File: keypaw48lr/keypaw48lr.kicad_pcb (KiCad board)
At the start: 2 copper layers, 139 x 102 mm, 108 parts, among them J1 Conn_01x02, J2 Conn_01x02, J3 Conn_01x02, J4 Conn_01x02, J5 Conn_01x02, J6 JD9613_OLED_FPC_Conn_01x10, J7 JD9613_OLED_FPC_Conn_01x10, J8 DXCL_S2002A_C, SW1 SW_SPDT, U1 nice_nano, U2 PAW3395, U3 TLV70019_SOT23-5, U4 TPS22917DBV

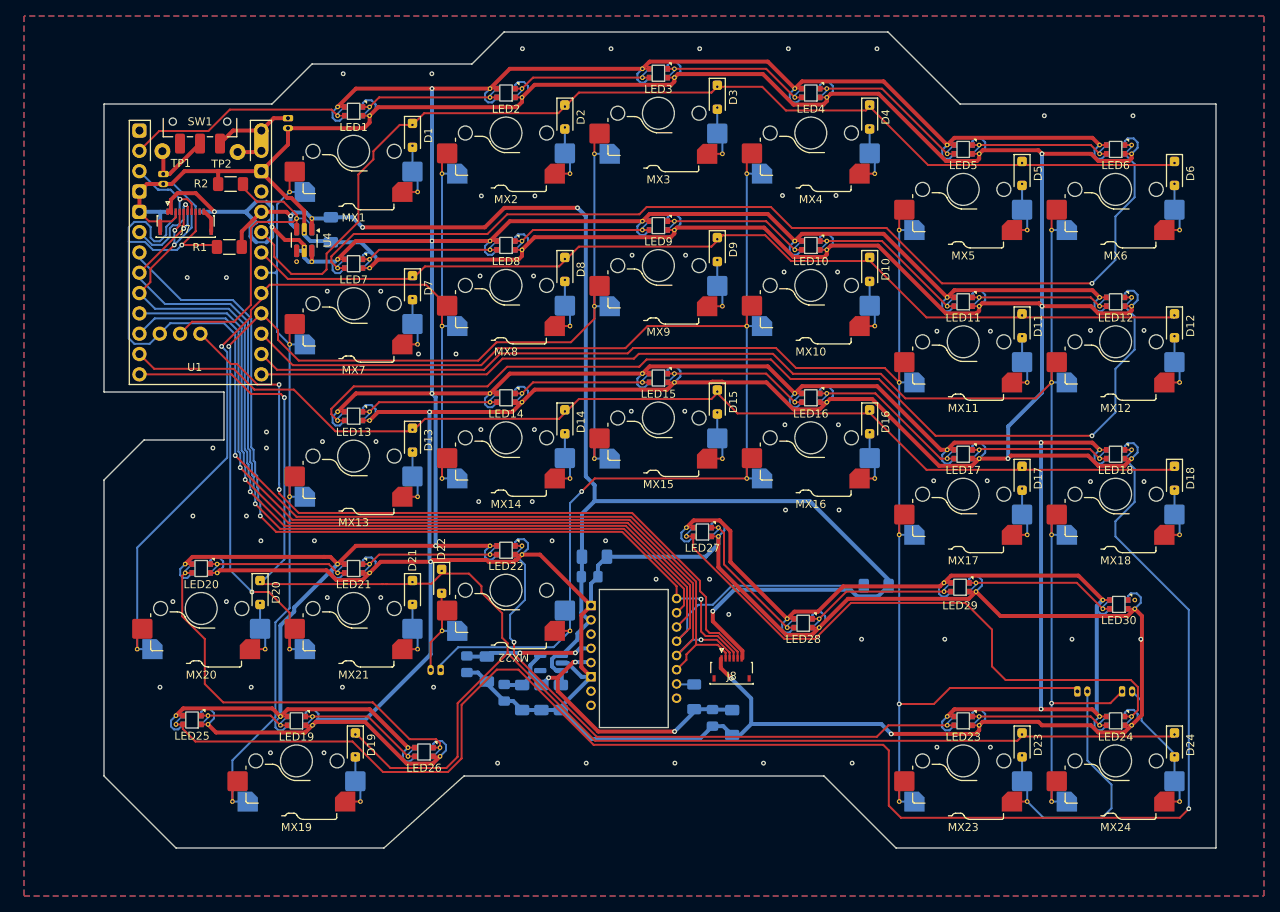
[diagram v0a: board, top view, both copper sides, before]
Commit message: feat: modify pcb for a simple box casing
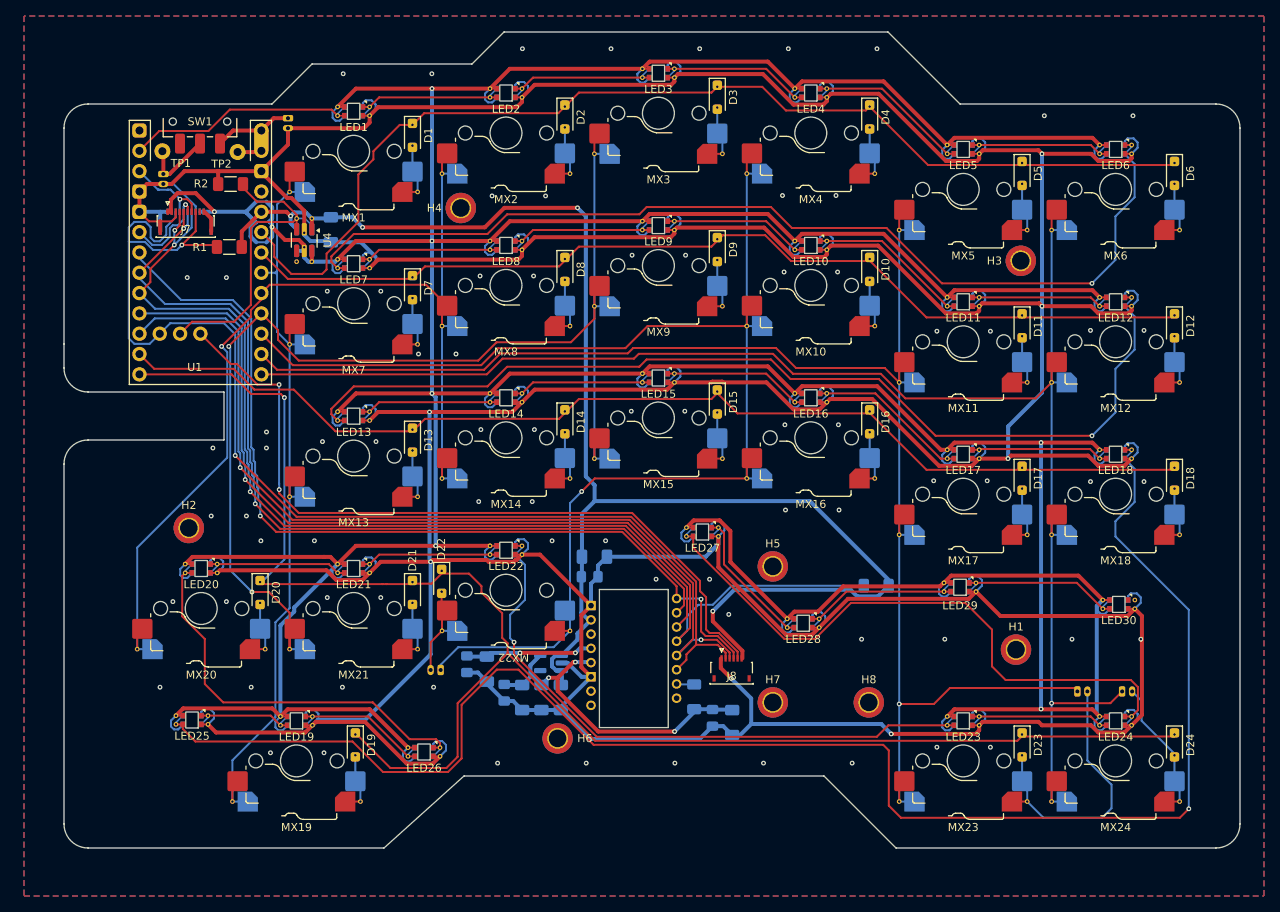
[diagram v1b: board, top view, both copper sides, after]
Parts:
- added H1: MountingHole, MountingHole:MountingHole_2.2mm_M2_DIN965_Pad_TopBottom, F.Cu at (159.0, 124.2)
- added H2: MountingHole, MountingHole:MountingHole_2.2mm_M2_DIN965_Pad_TopBottom, F.Cu at (55.6, 109.0)
- added H3: MountingHole, MountingHole:MountingHole_2.2mm_M2_DIN965_Pad_TopBottom, F.Cu at (159.6, 75.6)
- added H4: MountingHole, MountingHole:MountingHole_2.2mm_M2_DIN965_Pad_TopBottom, F.Cu at (89.6, 69.0)
- added H5: MountingHole, MountingHole:MountingHole_2.2mm_M2_DIN965_Pad_TopBottom, F.Cu at (128.6, 113.8)
- added H6: MountingHole, MountingHole:MountingHole_2.2mm_M2_DIN965_Pad_TopBottom, F.Cu at (101.7, 135.3)
- added H7: MountingHole, MountingHole:MountingHole_2.2mm_M2_DIN965_Pad_TopBottom, F.Cu at (128.6, 130.8)
- added H8: MountingHole, MountingHole:MountingHole_2.2mm_M2_DIN965_Pad_TopBottom, F.Cu at (140.6, 130.8)
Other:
- board size 139 x 102 mm -> 147 x 102 mm

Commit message: fix: route spi tracks out of antenna keepout zone
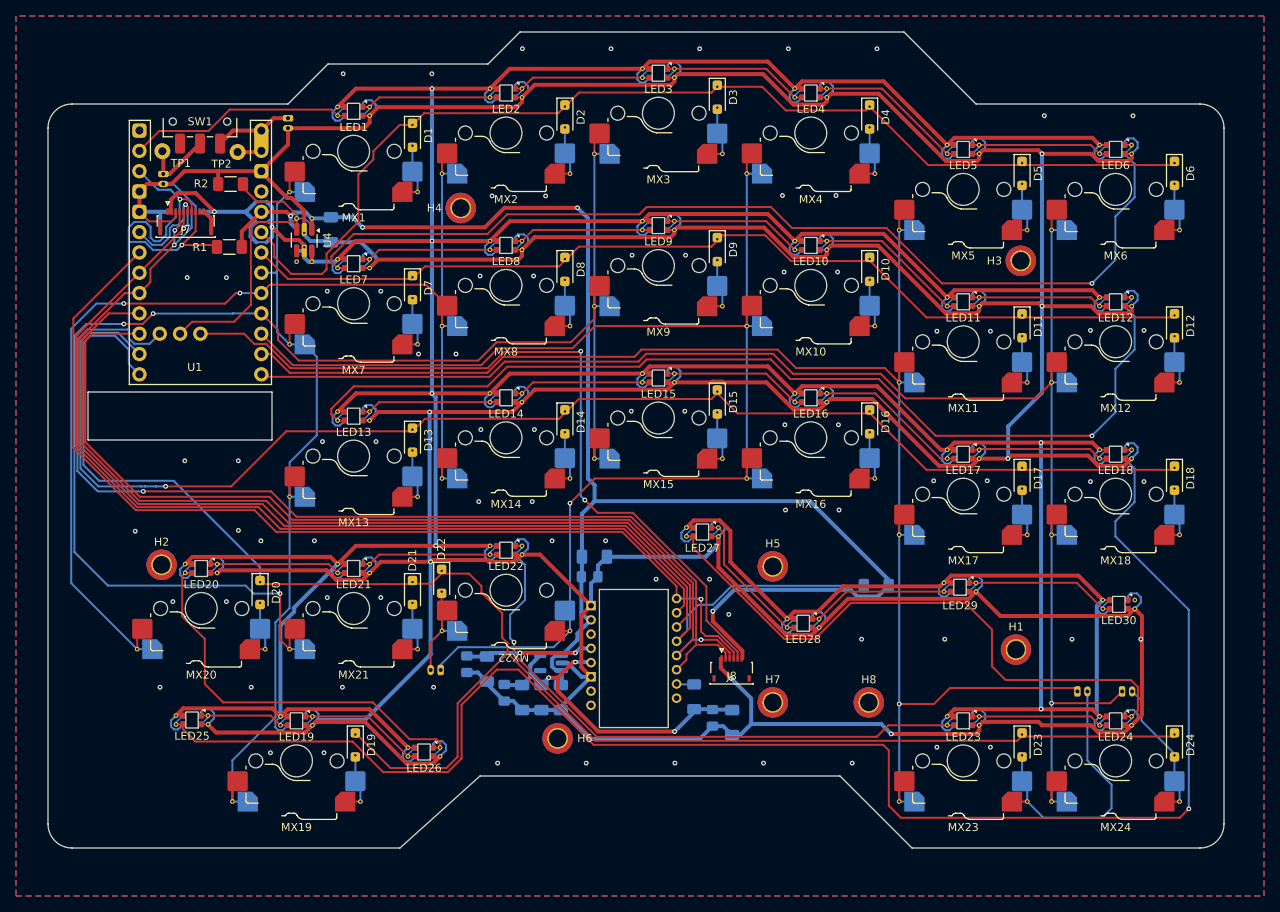
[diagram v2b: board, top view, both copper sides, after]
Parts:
- moved H2 5.72 mm to (52.2, 113.6)
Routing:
- net COL2: track 153.5 -> 192.3 mm, vias 2 -> 3
- net ROW2: track 139.4 -> 171.4 mm, vias 0 -> 1
- net COL1: track 133.2 -> 150.8 mm, vias 1 -> 2
- net NRESET: track 152.3 -> 169.0 mm
- net MOTION: track 113.2 -> 125.0 mm, vias 2 -> 1
- net ROW3: track 201.7 -> 212.8 mm, vias 1 -> 0
- net SDI: track 128.8 -> 139.9 mm, vias 1 -> 0
- net SDO: track 118.3 -> 129.3 mm, vias 3 -> 2
- net SCK: track 113.3 -> 123.9 mm, vias 2 -> 1
- net CS_PAW: track 112.3 -> 121.7 mm, vias 2 -> 1
- net EINT: track 95.5 -> 99.3 mm
- net COL0: track 101.7 -> 103.7 mm
- net GND: vias 85 -> 84
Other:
- outline, holes or cut-outs redrawn

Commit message: fix: reversible +BATT connector for left board
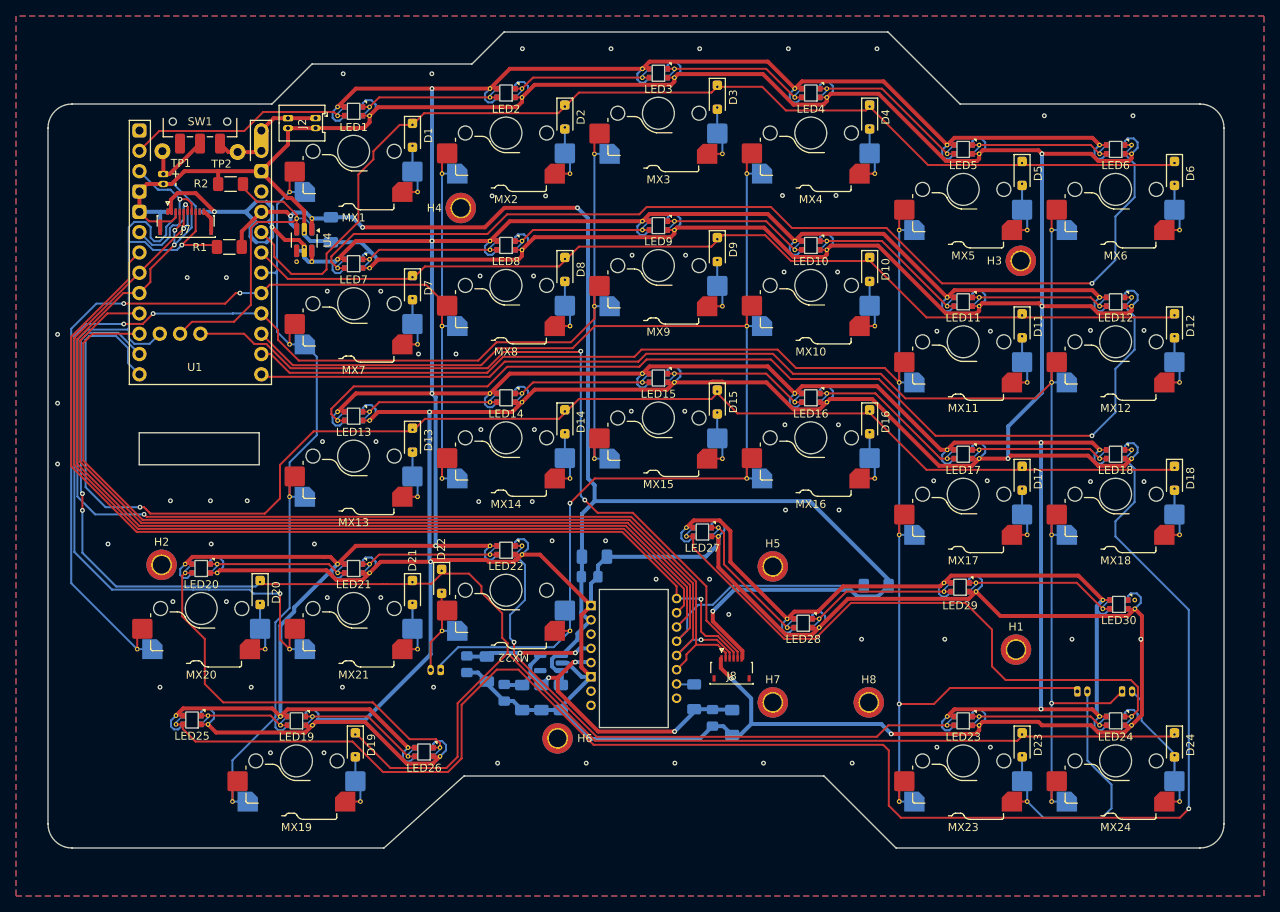
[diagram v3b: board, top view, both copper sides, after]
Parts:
- J1: footprint Connector_Molex:Molex_PicoBlade_53048-0210_1x02_P1.25mm_Horizontal -> MX_SW_HS_REV:Conn_1x02_P1.25mm_Horizontal_Battery
- J2: footprint Connector_Molex:Molex_PicoBlade_53048-0210_1x02_P1.25mm_Horizontal -> MX_SW_HS_REV:Conn_1x02_P1.25mm_Horizontal_Battery_REV
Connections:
- U1 pad 11: ROW2 -> ROW3
- U1 pad 12: ROW3 -> ROW2
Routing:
- net ROW2: track 171.4 -> 178.7 mm
- net ROW3: track 212.8 -> 217.5 mm, vias 0 -> 2
- net +BATT: track 13.1 -> 15.0 mm
- net NRESET: track 169.0 -> 170.9 mm
- net SDO: track 129.3 -> 131.2 mm
- net SDI: track 139.9 -> 141.7 mm
- net SCK: track 123.9 -> 125.6 mm
- net MOTION: track 125.0 -> 126.8 mm
- net CS_PAW: track 121.7 -> 123.5 mm
- net GND: vias 84 -> 87
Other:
- outline, holes or cut-outs redrawn

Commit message: chore: add a logo
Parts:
- added G***: LOGO, LOGO, F.Cu at (46.5, 132.9)
- added G***: LOGO, LOGO, B.Cu at (46.5, 132.9)
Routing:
- net GND: vias 87 -> 89
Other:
- board text added: "Keypaw v0.0.2"
